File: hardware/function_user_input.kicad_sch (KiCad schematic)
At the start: 17 parts, among them SW2 switch:SLB1470, SW3 SW_SP4T, SW4 SW_SP4T, SW5 SW_SP4T, SW6 SW_SPST, SW7 SW_SPST

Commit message: auto updated
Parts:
- renumbered R5 to R26, R6 to R27, R7 to R28, R8 to R29, R9 to R30, SW2 to SW3, SW3 to SW4, SW4 to SW5, SW5 to SW6, SW6 to SW7, SW7 to SW8

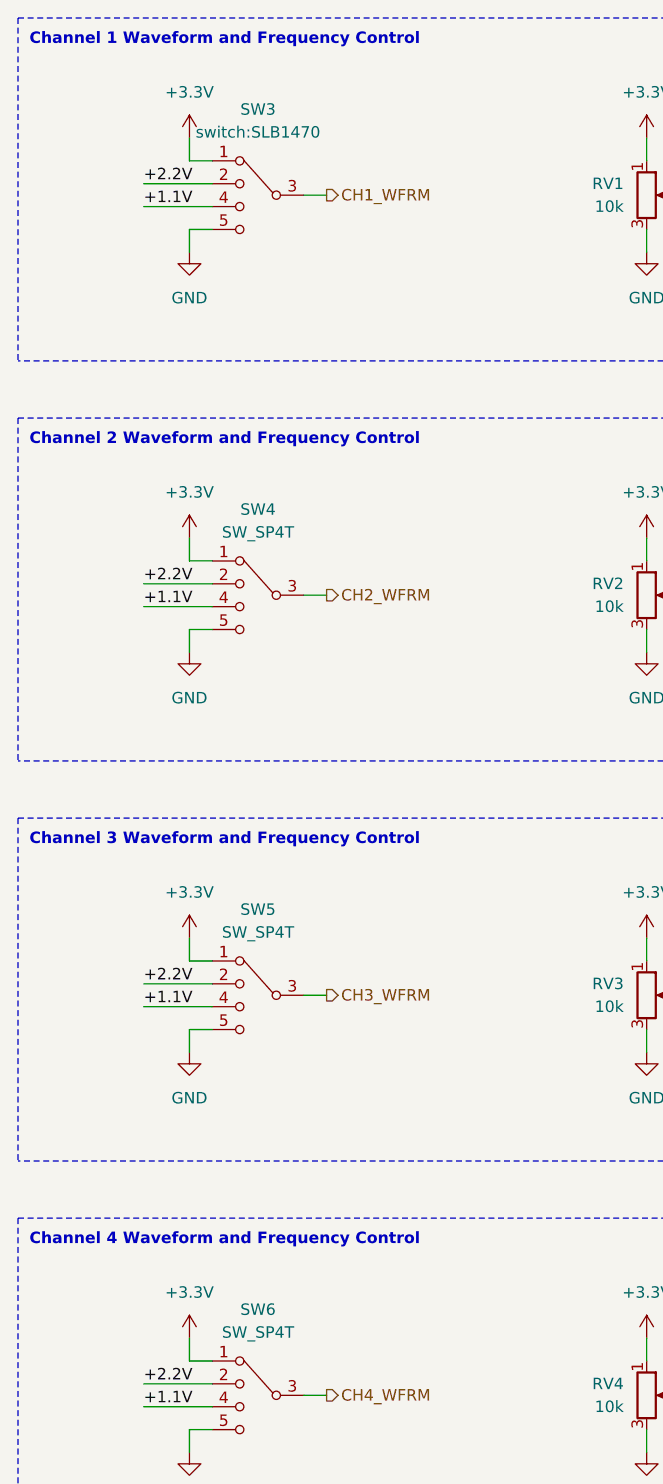
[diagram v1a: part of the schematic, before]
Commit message: update channel select footprint
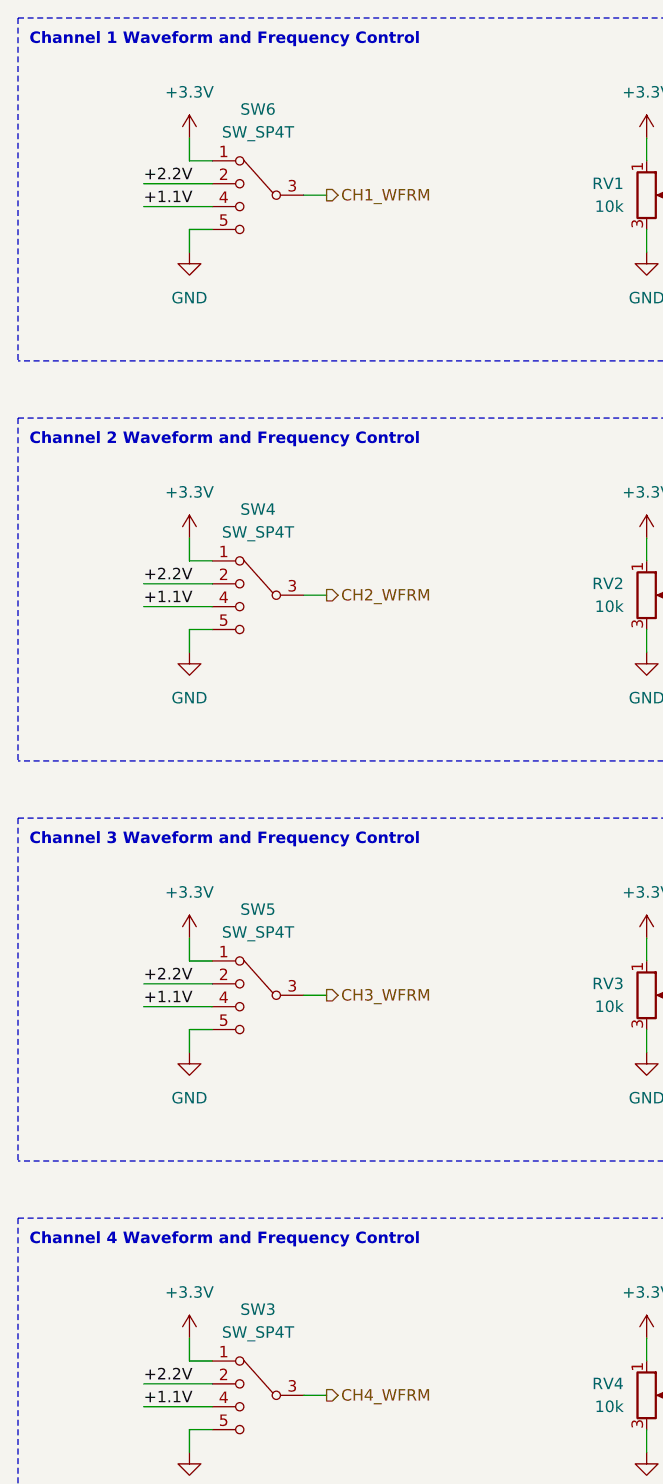
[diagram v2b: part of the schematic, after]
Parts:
- SW3: value switch:SLB1470 -> SW_SP4T
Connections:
- net CH1_WFRM: now also SW6.3; no longer SW3.3
- net CH4_WFRM: now also SW3.3; no longer SW6.3

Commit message: updated a footprint
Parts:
- SW7, SW8: footprint Button_Switch_THT:SW_CuK_JS202011CQN_DPDT_Straight -> Button_Switch_THT:SW_E-Switch_EG1271_SPDT
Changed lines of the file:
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@@
 			)
 		)
-		(property "Footprint" "Button_Switch_THT:SW_CuK_JS202011CQN_DPDT_Straight"
+		(property "Footprint" "Button_Switch_THT:SW_E-Switch_EG1271_SPDT"
 			(at 166.37 75.565 0)
 			(effects
@@
 			)
 		)
-		(property "Footprint" "Button_Switch_THT:SW_CuK_JS202011CQN_DPDT_Straight"
+		(property "Footprint" "Button_Switch_THT:SW_E-Switch_EG1271_SPDT"
 			(at 166.37 31.115 0)
 			(effects
